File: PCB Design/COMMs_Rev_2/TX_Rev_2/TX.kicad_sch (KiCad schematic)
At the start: 55 parts, among them J1 Conn_01x24_Pin, J2 Conn_01x24_Pin, J3 Conn_01x03_Pin, J4 Conn_01x04_Pin, Q1 IPD50N10S3L16ATMA1, Q2 IPD50N10S3L16ATMA1, Q3 IPD50N10S3L16ATMA1, Q4 IPD50N10S3L16ATMA1, U1 UCC27211AQDDARQ1, U2 UCC27211AQDDARQ1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

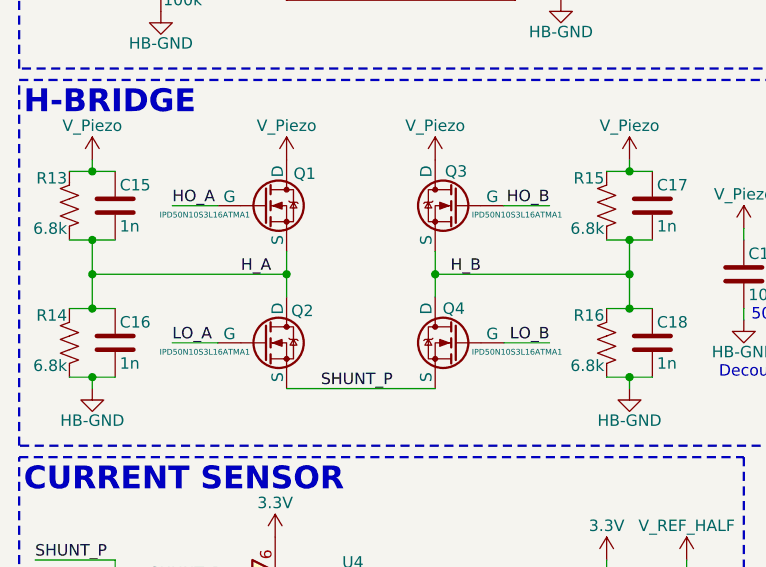
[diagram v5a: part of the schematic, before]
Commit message: Updated MOSFET
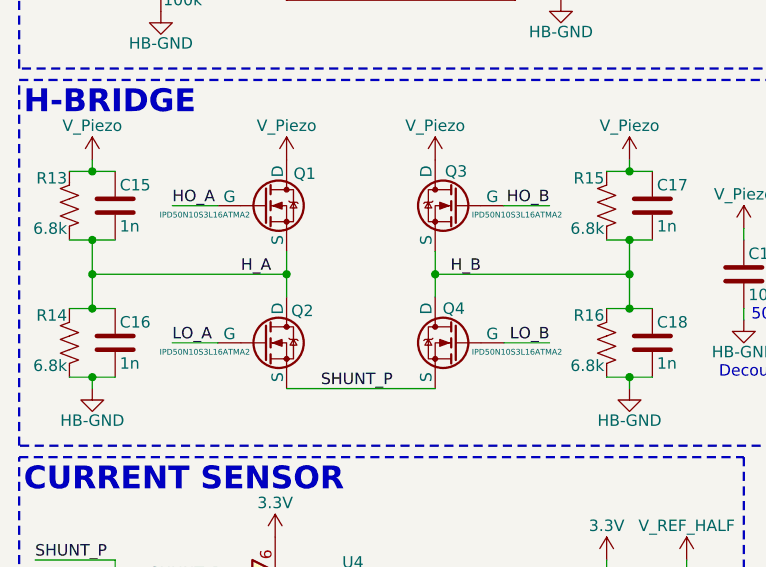
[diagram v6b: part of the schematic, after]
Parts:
- Q1, Q2, Q3, Q4: value IPD50N10S3L16ATMA1 -> IPD50N10S3L16ATMA2
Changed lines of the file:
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@@
 			)
 		)
-		(property "Value" "IPD50N10S3L16ATMA1"
+		(property "Value" "IPD50N10S3L16ATMA2"
 			(at 39.116 135.636 0)
 			(effects
@@
 			)
 		)
-		(property "Value" "IPD50N10S3L16ATMA1"
+		(property "Value" "IPD50N10S3L16ATMA2"
 			(at 39.116 120.396 0)
 			(effects
@@
 			)
 		)
-		(property "Value" "IPD50N10S3L16ATMA1"
+		(property "Value" "IPD50N10S3L16ATMA2"
 			(at 63.754 120.396 0)
 			(effects
@@
 			)
 		)
-		(property "Value" "IPD50N10S3L16ATMA1"
+		(property "Value" "IPD50N10S3L16ATMA2"
 			(at 63.754 135.636 0)
 			(effects
